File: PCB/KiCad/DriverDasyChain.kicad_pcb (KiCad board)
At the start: 4 copper layers, 70 x 70 mm, 35 parts, among them J1 Conn_01x02, J10 Conn_01x06, J12 Conn_01x03, J13 Conn_01x03, J16 Conn_01x02, J2 Conn_01x02, J4 Conn_01x04, J5 Conn_01x03, J7 Conn_01x07_Pin, J8 Conn_01x07_Pin, Q2 Q_NMOS_GDS, U1 AP2112K-3.3, U2 XIAO-ESP32-S3-DIP, U3 74AHCT1G125, U4 SN65HVD230

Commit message: Keine Änderungen vorgenommen.
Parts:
- removed J10: Conn_01x06, Connector_JST:JST_XH_B6B-XH-A_1x06_P2.50mm_Vertical
- added R5: 120, Resistor_SMD:R_0603_1608Metric_Pad0.98x0.95mm_HandSolder, F.Cu at (113.2, 68.8)
- added SW2: SW_DPST_x2, Button_Switch_SMD:SW_DIP_SPSTx01_Slide_6.7x4.1mm_W6.73mm_P2.54mm_LowProfile_JPin, F.Cu at (116.2, 64.7)
- C10: value 100p -> 1n
- J1, J2: value Conn_01x02 -> Conn_01x03
- moved C2 57.6 mm to (157.4, 50.8)
- moved C4 57.6 mm to (131.9, 46.3)
- moved C8 57.6 mm to (157.2, 40.8)
- moved C9 57.6 mm to (149.8, 41.0)
- moved D1 57.6 mm to (134.3, 40.9)
- moved Q2 57.6 mm to (143.3, 36.6)
- moved R3 57.6 mm to (152.7, 41.0)
- moved R4 57.6 mm to (132.1, 36.6)
- moved U1 57.6 mm to (157.3, 35.2)
- moved C3 57.6 mm to (146.6, 50.8)
- moved C5 57.6 mm to (162.5, 40.7)
- moved C6 57.6 mm to (162.5, 35.5)
- moved R2 57.6 mm to (136.5, 36.6)
- moved U3 57.6 mm to (151.0, 35.1)
- moved J8 44.5 mm to (120.0, 107.5), turned to 90 degrees
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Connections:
- net Net-(R2-Pad1) renamed /Treiber Out
- J1 pad 3: (no net) -> /CAN_SHLD
- J2 pad 3: (no net) -> /CAN_SHLD
- J7 pad 4: /<NO NET> -> /CAN TX
- J7 pad 5: Net-(J7-Pin_5) -> /CAN RX
- J7 pad 7: /GPIO RX (XIAO-ESP32-S3) -> unconnected-(J7-Pin_7-Pad7)
- J8 pad 1: /GPIO TX (XIAO-ESP32-S3) -> unconnected-(J8-Pin_1-Pad1)
- J8 pad 5: /GPIO A2 (XIAO-ESP32-S3) -> unconnected-(J8-Pin_5-Pad5)
- J8 pad 6: /GPIO A1 (XIAO-ESP32-S3) -> /<NO NET>
- J8 pad 7: /GPIO A0 (XIAO-ESP32-S3) -> /GPIO D0 (XIAO-ESP32-S3)
- R3 pad 1: Net-(J7-Pin_5) -> /GPIO D0 (XIAO-ESP32-S3)
- U3 pad 2: Net-(J7-Pin_5) -> /GPIO D0 (XIAO-ESP32-S3)
- U4 pad 1: /GPIO TX (XIAO-ESP32-S3) -> /CAN TX
- U4 pad 4: /GPIO RX (XIAO-ESP32-S3) -> /CAN RX
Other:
- board text removed: "R0192"

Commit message: Refactor PCB documentation for R0192 Daisy Chain Driverlink-PCB
- Updated the main documentation file `pcb_daisy_chain.md` to enhance clarity and structure, including detailed descriptions of functional blocks, design decisions, and GPIO assignments.
- Removed obsolete references to the MCP2515 and clarified the use of the SN65HVD230 CAN transceiver.
- Added detailed information on the brake control mechanism, including PWM control strategies and safety considerations.
- Introduced a new lock file for KiCad project management.
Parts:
- added D2: SMAJ5.0A, Diode_SMD:D_SMA, F.Cu at (122.6, 35.8)
- added D4: LED, LED_SMD:LED_0603_1608Metric_Pad1.05x0.95mm_HandSolder, F.Cu at (120.7, 39.3)
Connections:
- C4 pad 1: +48V -> GND
- C4 pad 2: GND -> +48V
- D1 pad 1: GND -> +48V
- D1 pad 2: /MOSFEST Out -> /MOSFET Out
- J1 pad 1: /CANL -> /CANH
- J1 pad 2: /CANH -> /CANL
- J16 pad 1: /MOSFEST Out -> Net-(J16-Pin_1)
- J16 pad 2: GND -> +48V
- J2 pad 1: /CANL -> /CANH
- J2 pad 2: /CANH -> /CANL
- J4 pad 1: /CANL -> /CANH
- J4 pad 2: /CANH -> /CANL
- J7 pad 7: unconnected-(J7-Pin_7-Pad7) -> /GPIO D7 (XIAO-ESP32-S3)
- J8 pad 1: unconnected-(J8-Pin_1-Pad1) -> /GPIO D6 (XIAO-ESP32-S3)
- J8 pad 2: unconnected-(J8-Pin_2-Pad2) -> /GPIO D5# (XIAO-ESP32-S3)
- J8 pad 4: unconnected-(J8-Pin_4-Pad4) -> /GPIO D3 (XIAO-ESP32-S3)
- J8 pad 6: /<NO NET> -> /GPIO D1 (XIAO-ESP32-S3)
- Q2 pad 2: /MOSFEST Out -> /MOSFET Out
- R5 pad 2: /CANL -> /CANH
- SW2 pad 2: /CANH -> /CANL
- U4 pad 6: /CANH -> /CANL
- U4 pad 7: /CANL -> /CANH

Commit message: Add SN74AHCT1G125 datasheet and update .DS_Store
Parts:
- added SW1: SW_DPST, Button_Switch_SMD:SW_DIP_SPSTx02_Slide_6.7x6.64mm_W6.73mm_P2.54mm_LowProfile_JPin, F.Cu at (100.7, 69.7)
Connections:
- R5 pad 1: Net-(SW2A-A) -> Net-(R5-Pad1)
- R5 pad 2: /CANH -> Net-(R5-Pad2)

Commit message: Refactor code structure for improved readability and maintainability
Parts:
- removed SW2: SW_DPST_x2, Button_Switch_SMD:SW_DIP_SPSTx01_Slide_6.7x4.1mm_W6.73mm_P2.54mm_LowProfile_JPin
- added C11: 100n, Capacitor_SMD:C_0603_1608Metric_Pad1.08x0.95mm_HandSolder, F.Cu at (95.7, 36.8)
- added C12: 100n, Capacitor_SMD:C_0603_1608Metric_Pad1.08x0.95mm_HandSolder, F.Cu at (95.7, 39.3)
- added J6: Conn_01x04, Connector_JST:JST_ZH_B4B-ZR_1x04_P1.50mm_Vertical, F.Cu at (124.8, 80.2)
- added R10: DNP, Resistor_SMD:R_0603_1608Metric_Pad0.98x0.95mm_HandSolder, F.Cu at (95.7, 51.8)
- added R11: R, Resistor_SMD:R_0603_1608Metric_Pad0.98x0.95mm_HandSolder, F.Cu at (95.7, 54.3)
- added R6: 1M, Resistor_SMD:R_0603_1608Metric_Pad0.98x0.95mm_HandSolder, F.Cu at (95.7, 41.8)
- added R7: 150k, Resistor_SMD:R_0603_1608Metric_Pad0.98x0.95mm_HandSolder, F.Cu at (95.7, 44.3)
- added R8: 10k, Resistor_SMD:R_0603_1608Metric_Pad0.98x0.95mm_HandSolder, F.Cu at (95.7, 46.8)
- added R9: 6.8k, Resistor_SMD:R_0603_1608Metric_Pad0.98x0.95mm_HandSolder, F.Cu at (95.7, 49.3)
- J16: footprint Connector_JST:JST_SH_SM02B-SRSS-TB_1x02-1MP_P1.00mm_Horizontal -> Connector_JST:JST_PH_S2B-PH-K_1x02_P2.00mm_Horizontal
- moved J16 93.8 mm to (177.6, 113.0), turned to 90 degrees
- moved J5 87.5 mm to (177.6, 89.0), turned to 90 degrees

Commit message: Refactor code structure for improved readability and maintainability
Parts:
- J1, J2: footprint Connector_Molex:Molex_Micro-Fit_3.0_43650-0300_1x03_P3.00mm_Horizontal -> TerminalBlock_Phoenix:TerminalBlock_Phoenix_PTSM-0,5-3-2.5-V-THR_1x03_P2.50mm_Vertical
- J12, J13: footprint Connector_AMASS:AMASS_MR30PW-M_1x03_P3.50mm_Horizontal -> TerminalBlock_WAGO:TerminalBlock_WAGO_2601-3104_1x04_P3.50mm_Vertical
- J16: footprint Connector_JST:JST_PH_S2B-PH-K_1x02_P2.00mm_Horizontal -> TerminalBlock_Phoenix:TerminalBlock_Phoenix_PTSM-0,5-2-2,5-V-SMD_1x02-1MP_P2.50mm_Vertical
- J4: footprint R0192:AMASS_XT30PW_2+2-M_1x04_P5.00mm_Horizontal -> TerminalBlock_WAGO:TerminalBlock_WAGO_2601-3104_1x04_P3.50mm_Vertical
- J5: footprint Connector_JST:JST_PH_S3B-PH-K_1x03_P2.00mm_Horizontal -> TerminalBlock_Phoenix:TerminalBlock_Phoenix_PTSM-0,5-3-2.5-V-THR_1x03_P2.50mm_Vertical
- J6: footprint Connector_JST:JST_ZH_B4B-ZR_1x04_P1.50mm_Vertical -> TerminalBlock_Phoenix:TerminalBlock_Phoenix_PTSM-0,5-4-2.5-V-THR_1x04_P2.50mm_Vertical
- moved J2 51.4 mm to (175.0, 112.0)
- moved J16 40.5 mm to (161.0, 76.0)
- moved J5 31.9 mm to (149.1, 74.5)
- moved J1 25.9 mm to (176.0, 88.0)
- moved J4 6.09 mm to (178.0, 104.2)
- moved J13 4.49 mm to (163.5, 124.0)
- moved J12 4.35 mm to (146.5, 124.0)

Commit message: Add DriverDasyChain schematic backup from September 8, 2026
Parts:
- removed D2: SMAJ5.0A, Diode_SMD:D_SMA
- removed J13: Conn_01x03, TerminalBlock_WAGO:TerminalBlock_WAGO_2601-3104_1x04_P3.50mm_Vertical
- removed J16: Conn_01x02, TerminalBlock_Phoenix:TerminalBlock_Phoenix_PTSM-0,5-2-2,5-V-SMD_1x02-1MP_P2.50mm_Vertical
- removed J7, J8: Conn_01x07_Pin, Connector_PinHeader_2.54mm:PinHeader_1x07_P2.54mm_Vertical
- removed JP1: Jumper_Resistor_120_Ohm, Resistor_SMD:R_0805_2012Metric
- removed R5: 120, Resistor_SMD:R_0603_1608Metric_Pad0.98x0.95mm_HandSolder
- added C13: 4.7n, Capacitor_SMD:C_0603_1608Metric_Pad1.08x0.95mm_HandSolder, F.Cu at (143.6, 95.1)
- added D3: SMAJ5.0CA, Diode_SMD:D_SMA, F.Cu at (156.4, 86.4)
- added F1: Polyfuse, Fuse:Fuse_Bourns_MF-RHT050, F.Cu at (178.2, 93.8)
- added J10: Conn_01x04, TerminalBlock_WAGO:TerminalBlock_WAGO_2601-3104_1x04_P3.50mm_Vertical, F.Cu at (146.8, 74.3)
- added J3: Conn_01x03, Connector_JST:JST_PH_B3B-PH-K_1x03_P2.00mm_Vertical, F.Cu at (180.4, 97.8)
- added R12: 60.4, Resistor_SMD:R_0603_1608Metric_Pad0.98x0.95mm_HandSolder, F.Cu at (141.0, 93.4)
- added R13: 60.4, Resistor_SMD:R_0603_1608Metric_Pad0.98x0.95mm_HandSolder, F.Cu at (141.0, 96.9)
- added SW3: SW_SPST, Button_Switch_SMD:SW_DIP_SPSTx01_Slide_Copal_CHS-01A_W5.08mm_P1.27mm_JPin, F.Cu at (136.2, 124.2)
- C6: value 1u -> 2.2u
- J12: value Conn_01x03 -> Conn_01x04
- J5: footprint TerminalBlock_Phoenix:TerminalBlock_Phoenix_PTSM-0,5-3-2.5-V-THR_1x03_P2.50mm_Vertical -> Connector_JST:JST_PH_B3B-PH-K_1x03_P2.00mm_Vertical
- J6: footprint TerminalBlock_Phoenix:TerminalBlock_Phoenix_PTSM-0,5-4-2.5-V-THR_1x04_P2.50mm_Vertical -> Connector_PinHeader_2.54mm:PinHeader_1x04_P2.54mm_Vertical
- R11: value R -> 470
- R8: value 10k -> 6.8k
- SW1: value SW_DPST -> SW_DIP_x02
- moved R9 101.5 mm to (161.9, 126.2)
- moved R11 95.8 mm to (161.9, 123.6)
- moved D4 95.4 mm to (165.5, 123.6), turned to 180 degrees
- moved C12 89.9 mm to (167.2, 93.8), turned to 90 degrees
- moved R7 89.9 mm to (170.1, 94.7), turned to 180 degrees
- moved C7 87.3 mm to (137.1, 120.9)
- moved R1 85.8 mm to (176.8, 115.1), turned to -90 degrees
- moved R8 84.0 mm to (165.3, 93.7), turned to 90 degrees
- moved U4 81.5 mm to (137.1, 116.1), turned to 90 degrees
- moved R4 78.9 mm to (167.5, 107.1), turned to -90 degrees
- moved C10 78.7 mm to (168.2, 124.7)
- moved R2 75.1 mm to (164.7, 106.2), turned to 0 degrees
- moved C1 71.7 mm to (176.8, 111.3), turned to -90 degrees
- moved U3 70.8 mm to (160.7, 105.2)
- moved Q2 70.7 mm to (172.1, 101.2)
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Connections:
- net /MOSFET Out renamed /BRAKE Out
- net /Treiber Out renamed /Driver Out
- C10 pad 1: /<NO NET> -> /TLE4905L Out
- J12 pad 1: GND -> +5V
- J12 pad 2: +48V -> GND
- J12 pad 3: +5V -> GND
- J12 pad 4: (no net) -> +48V
- J5 pad 1: +5V -> /TLE4905L Out
- J5 pad 2: /<NO NET> -> GND
- J5 pad 3: GND -> +5V
- Q2 pad 1: /<NO NET> -> /BRAKE GATE
- R1 pad 1: /<NO NET> -> /TLE4905L Out
- R11 pad 1: /GPIO D5# (XIAO-ESP32-S3) -> /GPIO D2 (XIAO-ESP32-S3)
- R2 pad 2: /<NO NET> -> /BRAKE GATE
- R4 pad 1: /<NO NET> -> /BRAKE GATE
- R9 pad 2: /<NO NET> -> /TLE4905L Out
- SW1 pad 1: /CANH -> /CANL
- SW1 pad 2: Net-(R5-Pad2) -> /CANH
- SW1 pad 3: /CANL -> /Endresistor CANH
- SW1 pad 4: Net-(R5-Pad1) -> /Endresistor CANL
- U2 pad 1: Net-(J11-Pin_7) -> /GPIO D0 (XIAO-ESP32-S3)
- U2 pad 10: Net-(J9-Pin_5) -> /CAN RX
- U2 pad 11: Net-(J9-Pin_4) -> /CAN TX
- U2 pad 13: Net-(J9-Pin_2) -> GND
- U2 pad 14: Net-(J9-Pin_1) -> unconnected-(U2-VBUS-Pad14)
- U2 pad 2: Net-(J11-Pin_6) -> /GPIO D1 (XIAO-ESP32-S3)
- U2 pad 3: Net-(J11-Pin_5) -> /GPIO D2 (XIAO-ESP32-S3)
- U2 pad 4: Net-(J11-Pin_4) -> /GPIO D3 (XIAO-ESP32-S3)
- U2 pad 5: Net-(J11-Pin_3) -> unconnected-(U2-GPIO5_A4_D4_SDA-Pad5)
- U2 pad 6: Net-(J11-Pin_2) -> unconnected-(U2-GPIO6_A5_D5_SCL-Pad6)
- U2 pad 7: Net-(J11-Pin_1) -> /GPIO D6 (XIAO-ESP32-S3)
- U2 pad 8: Net-(J9-Pin_7) -> /GPIO D7 (XIAO-ESP32-S3)
- U2 pad 9: Net-(J9-Pin_6) -> unconnected-(U2-GPIO7_A8_D8_SCK-Pad9)
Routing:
- net /CANH: track 0.00 -> 66.3 mm
- net /CANL: track 0.00 -> 58.1 mm
- net GND: track 0.03 -> 44.4 mm
- net /GPIO D3 (XIAO-ESP32-S3): track 0.00 -> 37.8 mm
- net +5V: track 0.00 -> 29.6 mm
- net /TLE4905L Out: track 0.00 -> 28.4 mm
- net /GPIO D0 (XIAO-ESP32-S3): track 0.00 -> 27.1 mm
- net +48V: track 0.14 -> 24.2 mm
- net /CAN_SHLD: track 0.00 -> 20.8 mm
- net /BRAKE Out: track 0.00 -> 17.1 mm
- net /GPIO D7 (XIAO-ESP32-S3): track 0.00 -> 14.6 mm
- net /CAN TX: track 0.00 -> 13.5 mm
- net +3.3V: track 0.00 -> 11.0 mm
- net /GPIO D6 (XIAO-ESP32-S3): track 0.00 -> 10.8 mm
- net /BRAKE +48V: track 0.00 -> 4.96 mm
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- added copper zone on In1.Cu, net GND

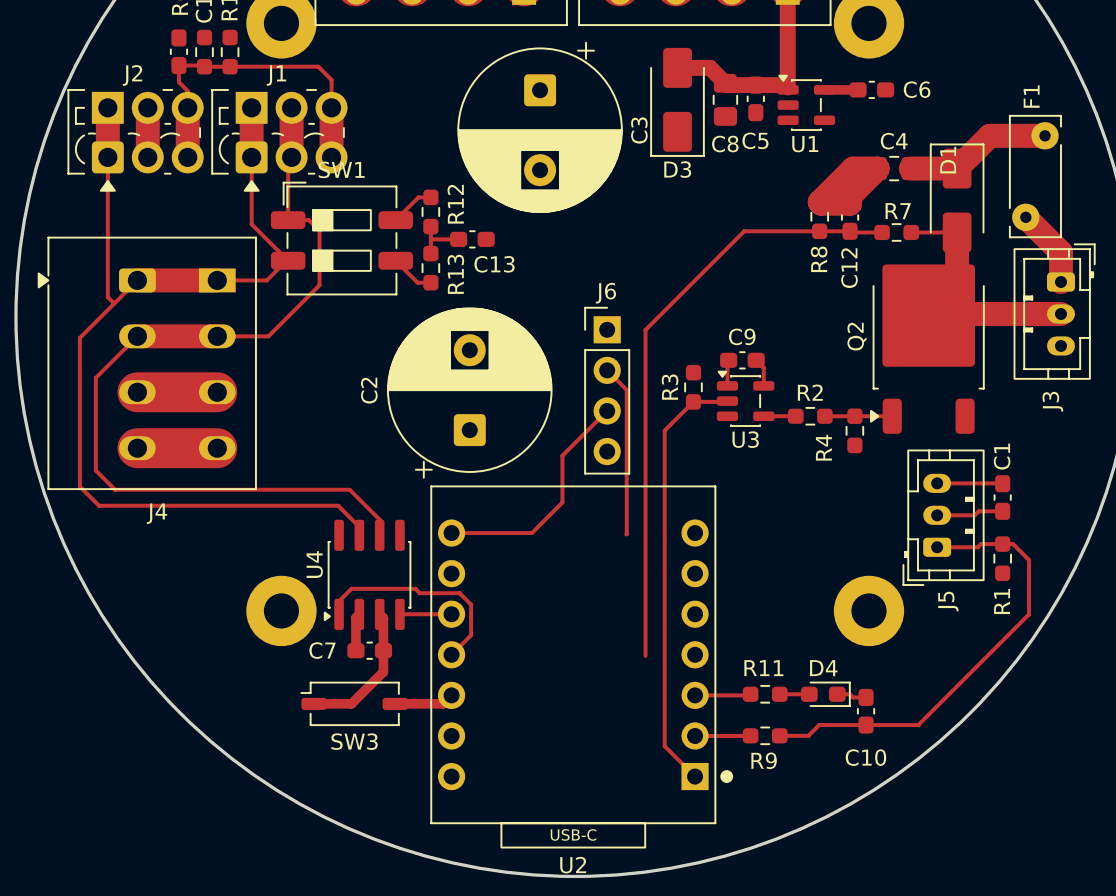
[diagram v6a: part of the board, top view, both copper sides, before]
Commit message: Add Mouser order list for PCB components
- Created a new CSV file containing the order details for various components needed for the PCB assembly.
- Included manufacturer names, part numbers, quantities, designators, descriptions, and additional notes for each component.
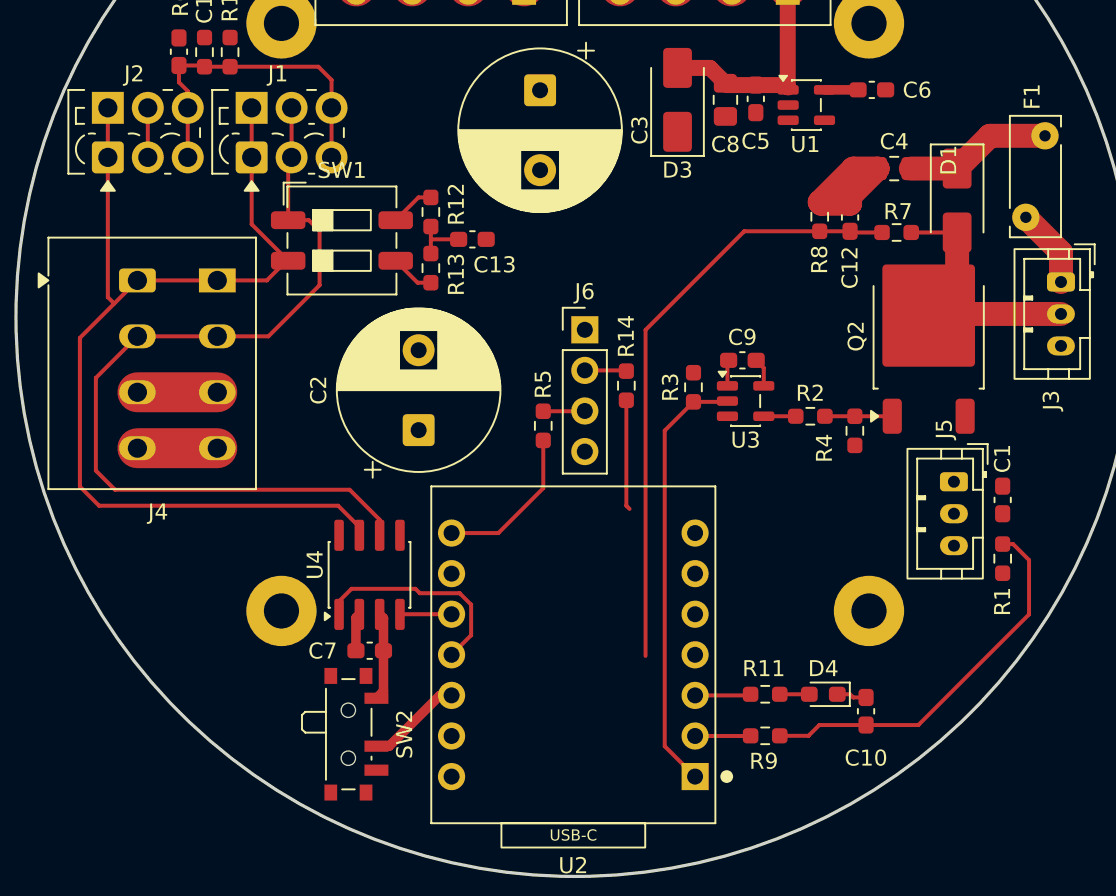
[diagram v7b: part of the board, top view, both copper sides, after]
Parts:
- removed SW3: SW_SPST, Button_Switch_SMD:SW_DIP_SPSTx01_Slide_Copal_CHS-01A_W5.08mm_P1.27mm_JPin
- added R14: 220, Resistor_SMD:R_0603_1608Metric_Pad0.98x0.95mm_HandSolder, F.Cu at (153.2, 104.3)
- added R5: 220, Resistor_SMD:R_0603_1608Metric_Pad0.98x0.95mm_HandSolder, F.Cu at (148.0, 106.8)
- added SW2: SW_SPDT, Button_Switch_SMD:SW_SPDT_PCM12, F.Cu at (136.1, 126.1)
- moved J5 4.23 mm to (173.7, 110.3), turned to -90 degrees
- moved C2 3.20 mm to (140.2, 107.1)
- moved J6 1.40 mm to (150.6, 100.8)
- moved C1 0.15 mm to (176.8, 111.4)
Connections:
- J5 pad 1: /TLE4905L Out -> +5V
- J5 pad 3: +5V -> /TLE4905L Out
- J6 pad 2: /GPIO D6 (XIAO-ESP32-S3) -> Net-(J6-Pin_2)
- J6 pad 3: /GPIO D7 (XIAO-ESP32-S3) -> Net-(J6-Pin_3)
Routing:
- net /GPIO D7 (XIAO-ESP32-S3): track 14.6 -> 9.89 mm
- net GND: track 44.4 -> 40.2 mm
- net /TLE4905L Out: track 28.4 -> 24.2 mm
- net +5V: track 29.6 -> 25.6 mm
- net /GPIO D6 (XIAO-ESP32-S3): track 10.8 -> 6.88 mm
- net +3.3V: track 11.0 -> 7.63 mm
- net Net-(J6-Pin_3): track 0.00 -> 2.63 mm
- net Net-(J6-Pin_2): track 0.00 -> 2.62 mm
- net Net-(SW2-B): track 3.74 -> 6.02 mm
